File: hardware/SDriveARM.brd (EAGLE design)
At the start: 43.2 x 43.2 mm, 46 parts, among them IC1 LD117AS33TR, SW1 IS-1290, U1 CY8C4245AXI-483

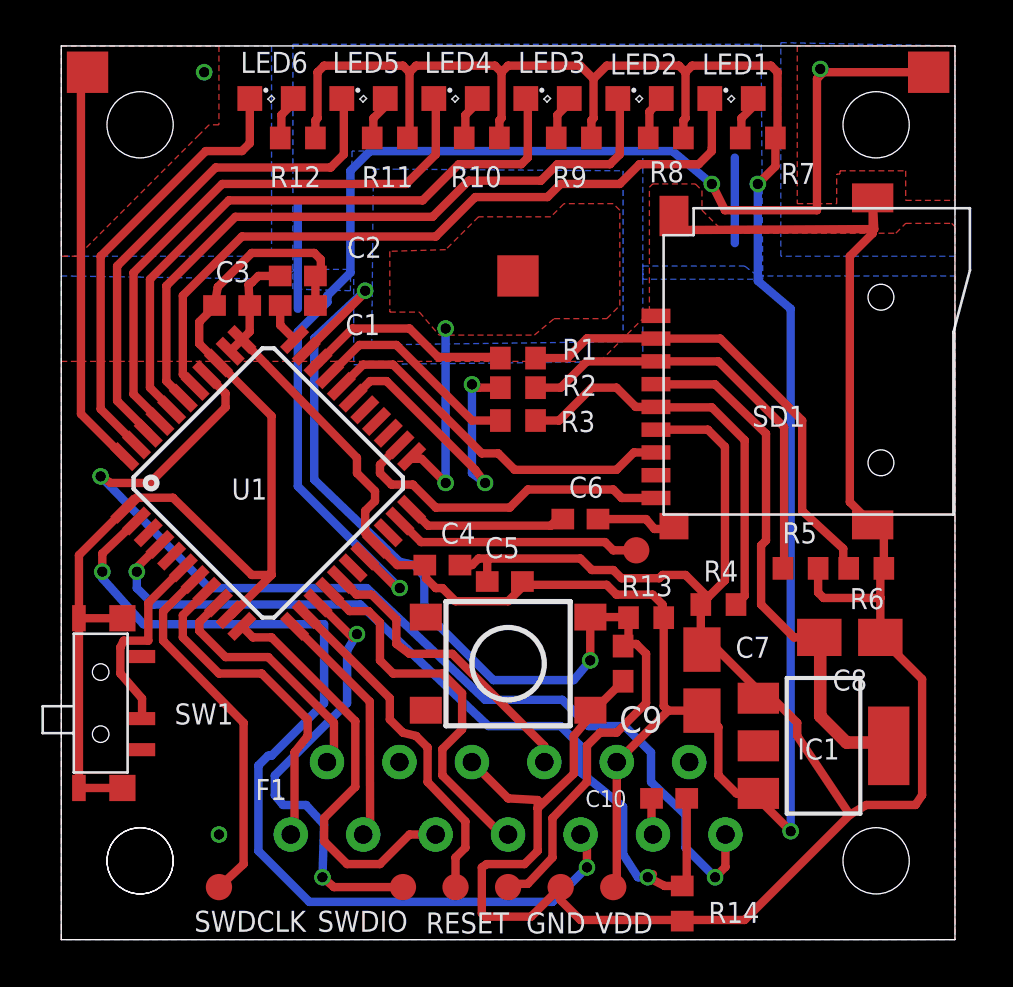
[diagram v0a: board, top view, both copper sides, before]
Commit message: Update HW design to v1.1
Add diode to "SIO data in" to allow work in chain
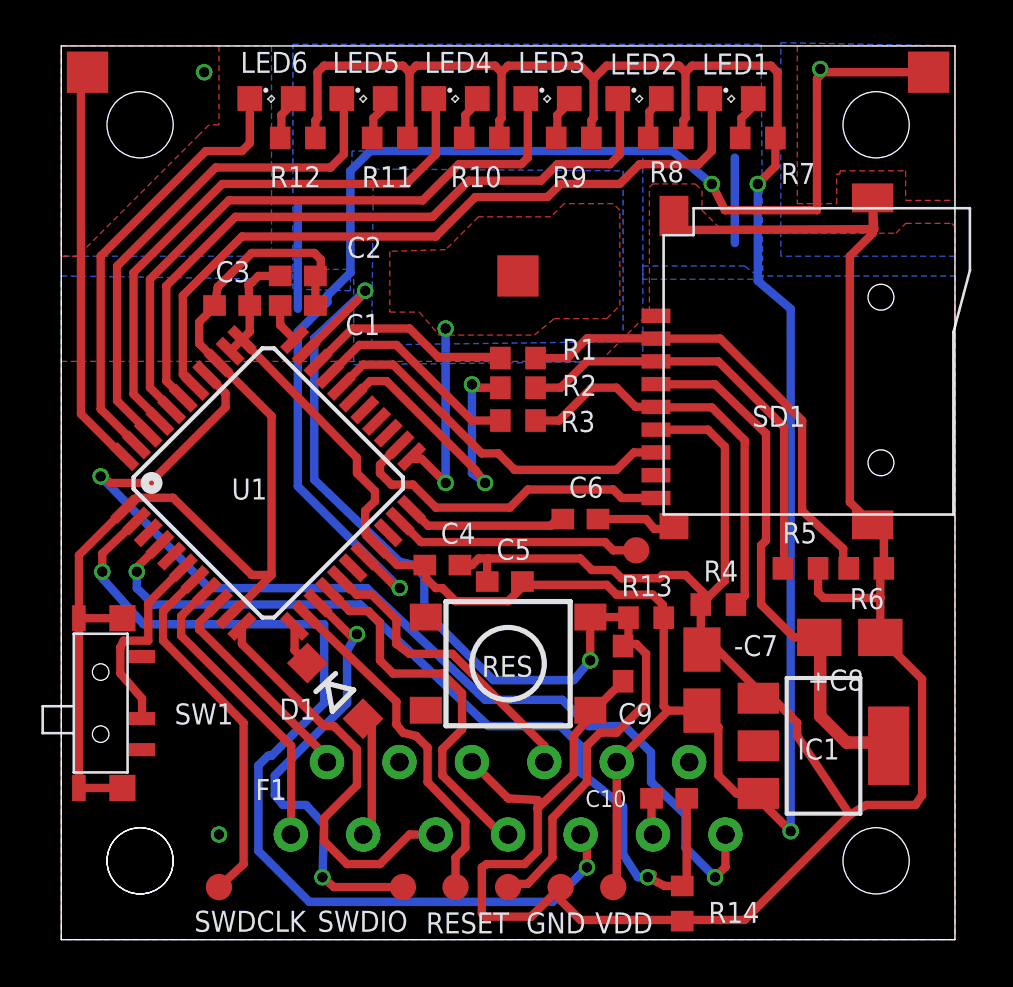
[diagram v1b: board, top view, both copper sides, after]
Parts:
- added D1: MBR0520LT, diode:SOD123
- renumbered C7 to -C7, C8 to +C8
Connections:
- new net N$3: D1.A, F1.3
- net P3_1: now also D1.C; no longer F1.3
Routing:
- net P3_1: track 11.7 -> 2.03 mm
- net N$3: track 0.00 -> 6.59 mm
- net P2_6: track 16.2 -> 14.5 mm
- net P2_7: track 12.3 -> 10.8 mm
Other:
- board text added: "RES"
- board text added: "SDriveARM v1.1 - 2017"
- board text removed: "SDriveARM v1.0 - 2016"
